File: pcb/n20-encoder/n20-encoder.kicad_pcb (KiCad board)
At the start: 2 copper layers, 10 x 18.2 mm, 9 parts, among them J1 CONN, M1 N20, U1 TLE4946-2K, U2 TLE4946-2K, U3 AH17x, U4 AH17x

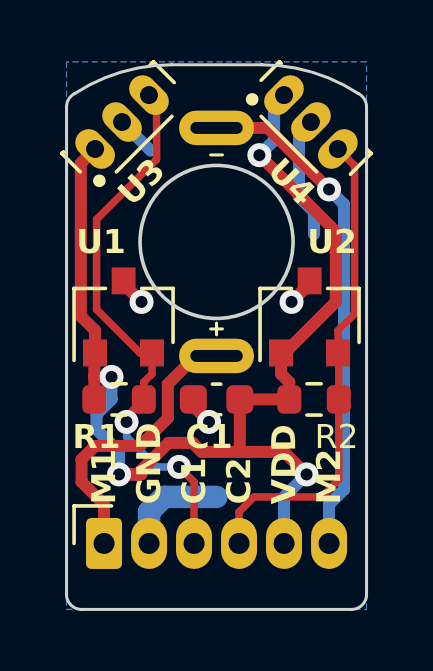
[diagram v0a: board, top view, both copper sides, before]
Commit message: Replace n20-encoder edge cuts hole with drill, improve routing
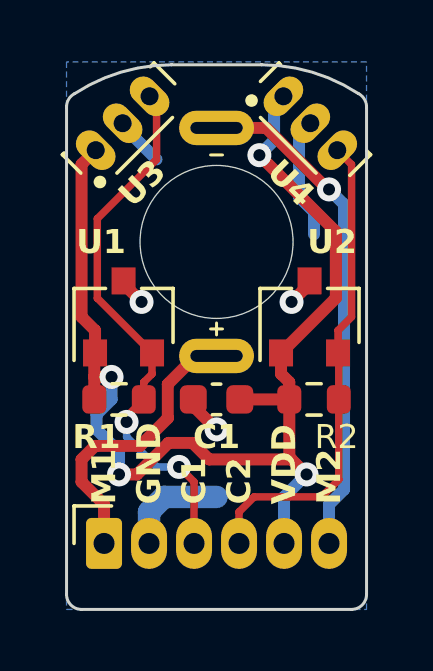
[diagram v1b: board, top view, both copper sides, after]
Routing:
- net VDD: track 39.5 -> 38.3 mm
- net /M1: track 9.70 -> 9.02 mm
- net /C1: track 18.6 -> 18.0 mm
